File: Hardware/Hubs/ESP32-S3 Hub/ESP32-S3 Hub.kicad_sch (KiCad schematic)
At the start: 23 parts, among them U1 ESP32-S3, Y1 ABM11-40.000MHZ-B1U-T3, 10ppm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

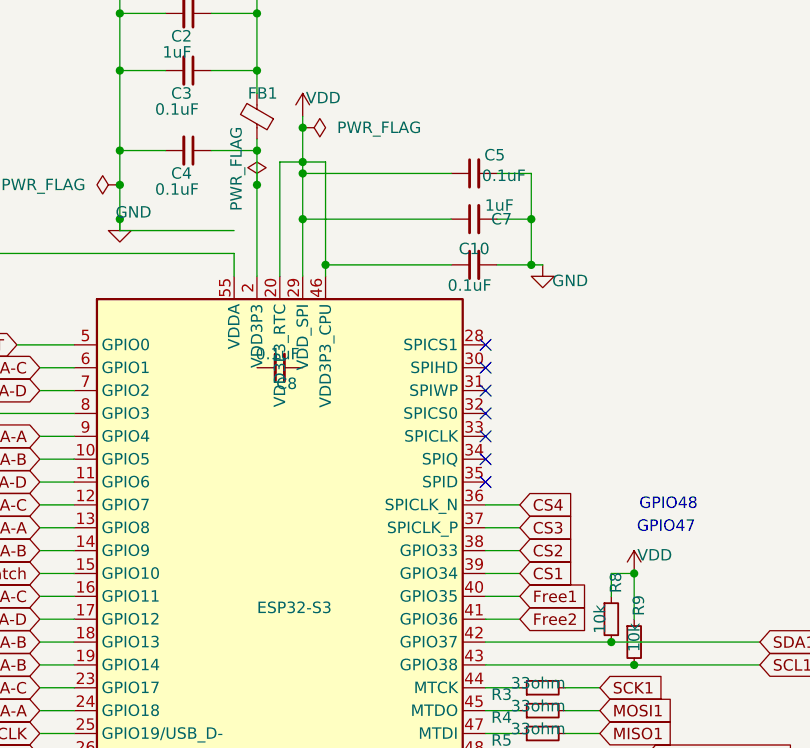
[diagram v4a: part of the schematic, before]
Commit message: Finished routing with current components
I may add some protection and isolation stuff
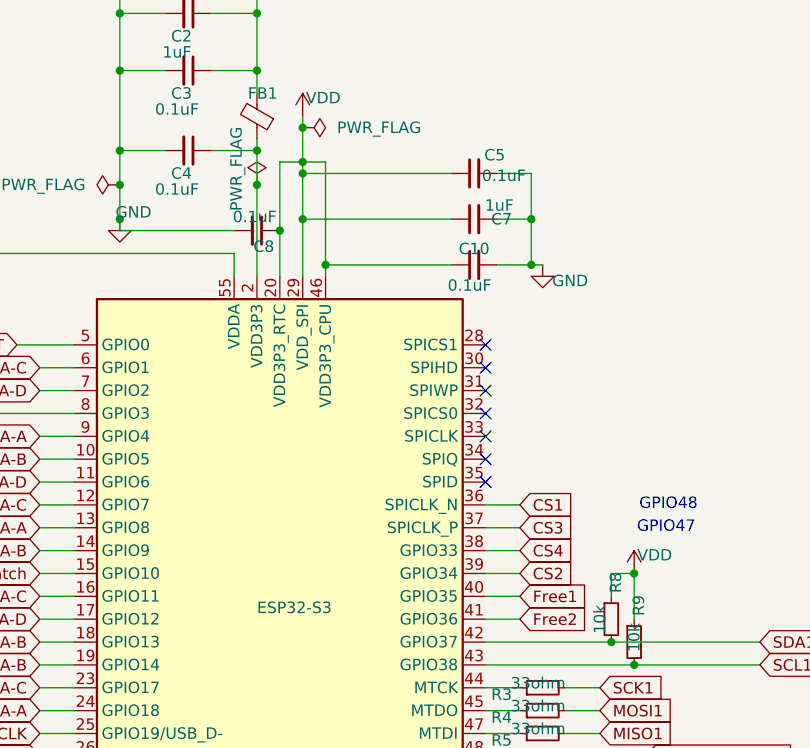
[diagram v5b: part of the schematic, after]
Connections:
- net CS1: now also U1.36 (SPICLK_N); no longer U1.39 (GPIO34)
- net CS2: now also U1.39 (GPIO34); no longer U1.38 (GPIO33)
- net CS4: now also U1.38 (GPIO33); no longer U1.36 (SPICLK_N)
- net GND: now also C8.2
- net VDD: now also C8.1
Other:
- moved on the sheet: C8
